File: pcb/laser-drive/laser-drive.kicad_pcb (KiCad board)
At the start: 2 copper layers, 28.6 x 32.4 mm, 28 parts, among them J1 CONN_01X03, P1 LaserOut, Q1 BCP5616Q, Q2 MTM232270, U2 MIC920

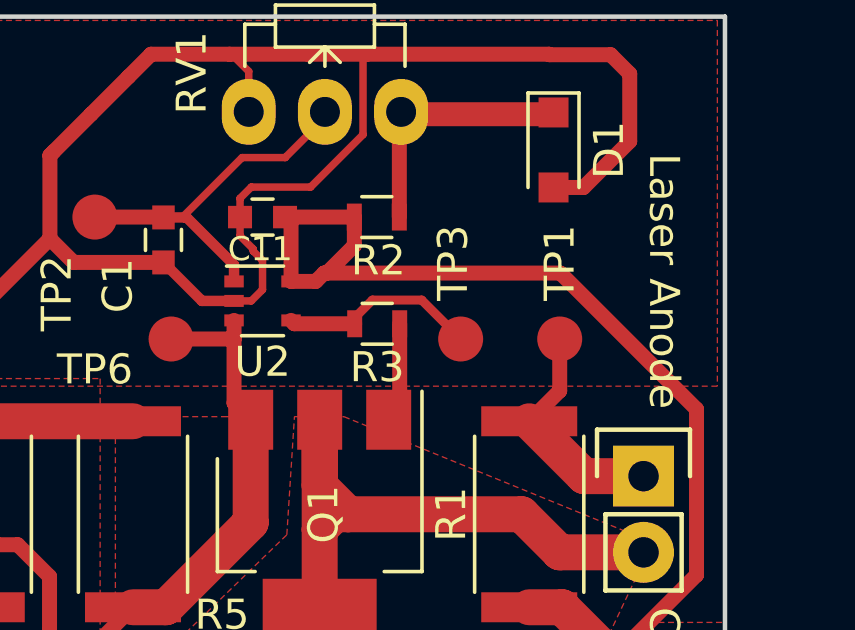
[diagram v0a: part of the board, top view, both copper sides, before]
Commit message: Add oscillation suppresion cap for laser driver.
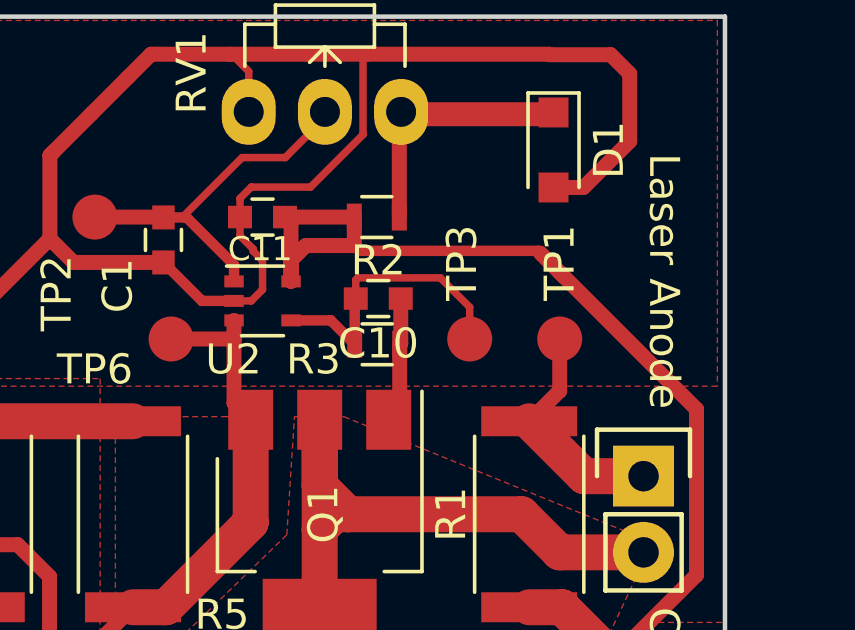
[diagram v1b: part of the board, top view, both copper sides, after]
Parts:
- added C10: 100p, Capacitors_SMD:C_0603, F.Cu at (100.2, 54.5)
- moved R3 0.68 mm to (100.2, 56.0)
- moved TP3 0.30 mm to (103.3, 55.8)
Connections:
- net /ControlOut renamed Net-(C10-Pad2)
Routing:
- net Net-(C10-Pad2): track 6.84 -> 9.93 mm
- net Net-(C10-Pad1): track 3.35 -> 4.21 mm

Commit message: o work in progress.
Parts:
- removed the C5 at (98.1, 75.0)
- removed the C6 at (93.7, 69.9)
- removed the C7 at (98.1, 69.9)
- removed C8: 10u, Capacitors_SMD:C_1210
- removed C9: 100n, Capacitors_SMD:C_0805
- added C2: 100n, Capacitors_SMD:C_0603, F.Cu at (106.2, 73.2)
- added REF**: MountingHole_3.2mm_M3, Mounting_Holes:MountingHole_3.2mm_M3, F.Cu at (94.0, 73.7)
- added REF**: MountingHole_3.2mm_M3, Mounting_Holes:MountingHole_3.2mm_M3, F.Cu at (108.0, 53.3)
- J1: footprint Pin_Headers:Pin_Header_Straight_1x03_Pitch2.54mm -> Pin_Headers:Pin_Header_Straight_1x03_Pitch2.00mm
- P1: footprint Pin_Headers:Pin_Header_Straight_1x02 -> Connectors_JST:JST_XH_B02B-XH-A_02x2.50mm_Straight
- TP1: value Current -> Curr
- TP3: value Control-Out -> Ctrl
- moved TP3 21.8 mm to (124.1, 62.1)
- moved R8 17.1 mm to (106.2, 75.9), turned to 0 degrees
- moved TP6 17.0 mm to (76.3, 57.0)
- moved J1 14.2 mm to (99.1, 75.9), turned to 90 degrees
- moved R3 11.5 mm to (91.2, 63.2), turned to 270 degrees
- moved TP2 10.8 mm to (80.5, 48.3)
- moved C6 10.3 mm to (91.2, 59.4), turned to 270 degrees
- moved Q2 10.1 mm to (99.1, 72.1), turned to 270 degrees
- moved R7 9.79 mm to (94.2, 68.1), turned to 0 degrees
- moved R6 9.61 mm to (99.3, 68.8), turned to 270 degrees
- moved R1 9.39 mm to (102.4, 70.6)
- moved D1 6.77 mm to (102.6, 55.4), turned to 90 degrees
- moved R2 5.69 mm to (95.8, 55.4)
- moved TP1 4.52 mm to (110.5, 57.4)
- moved C7 4.36 mm to (98.8, 55.4)
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- renumbered C2 to C3, C3 to C4, C4 to C5, C10 to C6, C11 to C7
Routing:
- net GND: track 130.9 -> 0.00 mm
- net +12V: track 85.8 -> 0.00 mm, vias 2 -> 0
- net /LaserOut: track 21.4 -> 0.00 mm
- net /VSense: track 17.0 -> 0.00 mm
- net /VRef: track 12.8 -> 0.00 mm
- net Net-(C6-Pad2): track 9.93 -> 0.00 mm
- net Net-(D1-Pad1): track 9.19 -> 0.00 mm
- net /CurrentTP: track 7.73 -> 0.00 mm
- net Net-(Q2-Pad3): track 6.55 -> 0.00 mm
- net Net-(R5-Pad2): track 5.21 -> 0.00 mm
- net Net-(J1-Pad2): track 4.56 -> 0.00 mm
- net Net-(C6-Pad1): track 4.21 -> 0.00 mm
- removed copper zone on F.Cu, net +12V
- removed copper zone on F.Cu, net /LaserOut
- removed copper zone on F.Cu, net /VSense
- removed copper zone on F.Cu, net GND
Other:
- board size 28.6 x 32.4 mm -> 21.6 x 27.9 mm

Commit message: playing with placement.
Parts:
- moved TP1 11.4 mm to (121.9, 57.7)
- moved R8 8.88 mm to (101.7, 68.3), turned to 90 degrees
- moved C3 7.94 mm to (104.9, 68.3), turned to 180 degrees
- moved R1 7.28 mm to (109.6, 69.6)
- moved C5 7.01 mm to (108.9, 75.5), turned to 180 degrees
- moved C4 5.53 mm to (104.9, 71.8), turned to 180 degrees
- moved C2 2.44 mm to (105.7, 75.5), turned to 270 degrees
- moved P1 0.97 mm to (107.6, 62.5)
- moved J1 0.50 mm to (98.6, 75.7)
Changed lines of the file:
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@@
 )
 (setup
-  (last_trace_width 0.3)
+  (last_trace_width 0.25)
   (user_trace_width 0.25)
   (user_trace_width 0.3)
@@
 )
   (module Capacitors_SMD:C_0603 (layer F.Cu)
-    (at 106.172 73.152)
+    (at 105.664 75.5396 270)
     (descr "Capacitor SMD 0603, reflow soldering, AVX (see smccp.pdf)")
     (tags "capacitor 0603")
     (attr smd)
-    (fp_text reference C2 (at 0 -1.5) (layer F.SilkS)
-      (effects (font (size 1 1) (thickness 0.15)))
-    )
-    (fp_text value 100n (at 0 1.5) (layer F.Fab)
+    (fp_text reference C2 (at 0 -1.5 270) (layer F.SilkS)
+      (effects (font (size 1 1) (thickness 0.15)))
+    )
+    (fp_text value 100n (at 0 1.5 270) (layer F.Fab)
       (effects (font (size 1 1) (thickness 0.15)))
     )
@@
     (fp_line (start 0.8 0.4) (end -0.8 0.4) (layer F.Fab) (width 0.1))
     (fp_line (start -0.8 0.4) (end -0.8 -0.4) (layer F.Fab) (width 0.1))
-    (fp_text user %R (at 0 0) (layer F.Fab)
+    (fp_text user %R (at 0 0 270) (layer F.Fab)
       (effects (font (size 0.3 0.3) (thickness 0.075)))
     )
-    (pad 2 smd rect (at 0.75 0) (size 0.8 0.75) (layers F.Cu F.Paste F.Mask)
-      (net 1 GND))
-    (pad 1 smd rect (at -0.75 0) (size 0.8 0.75) (layers F.Cu F.Paste F.Mask)
+    (pad 2 smd rect (at 0.75 0 270) (size 0.8 0.75) (layers F.Cu F.Paste F.Mask)
+      (net 1 GND))
+    (pad 1 smd rect (at -0.75 0 270) (size 0.8 0.75) (layers F.Cu F.Paste F.Mask)
       (net 2 +12V))
     (model Capacitors_SMD.3dshapes/C_0603.wrl
@@
   )
   (module Pin_Headers:Pin_Header_Straight_1x03_Pitch2.00mm (layer F.Cu)
-    (at 99.06 75.946 90)
+    (at 98.6028 75.7428 90)
     (descr "Through hole straight pin header, 1x03, 2.00mm pitch, single row")
     (tags "Through hole pin header THT 1x03 2.00mm single row")
@@
   )
   (module Connectors_JST:JST_XH_B02B-XH-A_02x2.50mm_Straight (layer F.Cu)
-    (at 107.569 63.5 90)
+    (at 107.5944 62.5348 90)
     (descr "JST XH series connector, B02B-XH-A, top entry type, through hole")
     (tags "connector jst xh tht top vertical 2.50mm")
@@
   )
   (module Capacitors_SMD:C_1210 (layer F.Cu)
-    (at 109.728 69.088 90)
+    (at 104.902 71.7804 180)
     (descr "Capacitor SMD 1210, reflow soldering, AVX (see smccp.pdf)")
     (tags "capacitor 1210")
     (attr smd)
-    (fp_text reference C4 (at 0 -2.25 90) (layer F.SilkS)
-      (effects (font (size 1 1) (thickness 0.15)))
-    )
-    (fp_text value 10u (at 0 2.5 90) (layer F.Fab)
+    (fp_text reference C4 (at 0 -2.25 180) (layer F.SilkS)
+      (effects (font (size 1 1) (thickness 0.15)))
+    )
+    (fp_text value 10u (at 0 2.5 180) (layer F.Fab)
       (effects (font (size 1 1) (thickness 0.15)))
     )
@@
     (fp_line (start 1.6 1.25) (end -1.6 1.25) (layer F.Fab) (width 0.1))
     (fp_line (start -1.6 1.25) (end -1.6 -1.25) (layer F.Fab) (width 0.1))
-    (fp_text user %R (at 0 -2.25 90) (layer F.Fab)
-      (effects (font (size 1 1) (thickness 0.15)))
-    )
-    (pad 2 smd rect (at 1.5 0 90) (size 1 2.5) (layers F.Cu F.Paste F.Mask)
-      (net 1 GND))
-    (pad 1 smd rect (at -1.5 0 90) (size 1 2.5) (layers F.Cu F.Paste F.Mask)
+    (fp_text user %R (at 0 -2.25 180) (layer F.Fab)
+      (effects (font (size 1 1) (thickness 0.15)))
+    )
+    (pad 2 smd rect (at 1.5 0 180) (size 1 2.5) (layers F.Cu F.Paste F.Mask)
+      (net 1 GND))
+    (pad 1 smd rect (at -1.5 0 180) (size 1 2.5) (layers F.Cu F.Paste F.Mask)
       (net 2 +12V))
     (model Capacitors_SMD.3dshapes/C_1210.wrl
@@
   )
   (module Capacitors_SMD:C_1210 (layer F.Cu)
-    (at 106.172 69.088 90)
+    (at 108.9152 75.5396 180)
     (descr "Capacitor SMD 1210, reflow soldering, AVX (see smccp.pdf)")
     (tags "capacitor 1210")
     (attr smd)
-    (fp_text reference C5 (at 0 -2.25 90) (layer F.SilkS)
-      (effects (font (size 1 1) (thickness 0.15)))
-    )
-    (fp_text value 10u (at 0 2.5 90) (layer F.Fab)
-      (effects (font (size 1 1) (thickness 0.15)))
-    )
-    (fp_text user %R (at 0 -2.25 90) (layer F.Fab)
+    (fp_text reference C5 (at 0 -2.25 180) (layer F.SilkS)
+      (effects (font (size 1 1) (thickness 0.15)))
+    )
+    (fp_text value 10u (at 0 2.5 180) (layer F.Fab)
+      (effects (font (size 1 1) (thickness 0.15)))
+    )
+    (fp_text user %R (at 0 -2.25 180) (layer F.Fab)
       (effects (font (size 1 1) (thickness 0.15)))
     )
@@
     (fp_line (start 2.25 1.5) (end 2.25 -1.5) (layer F.CrtYd) (width 0.05))
     (fp_line (start 2.25 1.5) (end -2.25 1.5) (layer F.CrtYd) (width 0.05))
-    (pad 1 smd rect (at -1.5 0 90) (size 1 2.5) (layers F.Cu F.Paste F.Mask)
+    (pad 1 smd rect (at -1.5 0 180) (size 1 2.5) (layers F.Cu F.Paste F.Mask)
       (net 2 +12V))
-    (pad 2 smd rect (at 1.5 0 90) (size 1 2.5) (layers F.Cu F.Paste F.Mask)
+    (pad 2 smd rect (at 1.5 0 180) (size 1 2.5) (layers F.Cu F.Paste F.Mask)
       (net 1 GND))
     (model Capacitors_SMD.3dshapes/C_1210.wrl
@@
   )
   (module Capacitors_SMD:C_1210 (layer F.Cu)
-    (at 109.601 74.676 270)
+    (at 104.902 68.2752 180)
     (descr "Capacitor SMD 1210, reflow soldering, AVX (see smccp.pdf)")
     (tags "capacitor 1210")
     (attr smd)
-    (fp_text reference C3 (at 0 -2.25 270) (layer F.SilkS)
-      (effects (font (size 1 1) (thickness 0.15)))
-    )
-    (fp_text value 10u (at 0 2.5 270) (layer F.Fab)
-      (effects (font (size 1 1) (thickness 0.15)))
-    )
-    (fp_text user %R (at 0 -2.25 270) (layer F.Fab)
+    (fp_text reference C3 (at 0 -2.25 180) (layer F.SilkS)
+      (effects (font (size 1 1) (thickness 0.15)))
+    )
+    (fp_text value 10u (at 0 2.5 180) (layer F.Fab)
+      (effects (font (size 1 1) (thickness 0.15)))
+    )
+    (fp_text user %R (at 0 -2.25 180) (layer F.Fab)
       (effects (font (size 1 1) (thickness 0.15)))
     )
@@
     (fp_line (start 2.25 1.5) (end 2.25 -1.5) (layer F.CrtYd) (width 0.05))
     (fp_line (start 2.25 1.5) (end -2.25 1.5) (layer F.CrtYd) (width 0.05))
-    (pad 1 smd rect (at -1.5 0 270) (size 1 2.5) (layers F.Cu F.Paste F.Mask)
+    (pad 1 smd rect (at -1.5 0 180) (size 1 2.5) (layers F.Cu F.Paste F.Mask)
       (net 2 +12V))
-    (pad 2 smd rect (at 1.5 0 270) (size 1 2.5) (layers F.Cu F.Paste F.Mask)
+    (pad 2 smd rect (at 1.5 0 180) (size 1 2.5) (layers F.Cu F.Paste F.Mask)
       (net 1 GND))
     (model Capacitors_SMD.3dshapes/C_1210.wrl
@@
   )
   (module Measurement_Points:Measurement_Point_Round-SMD-Pad_Small (layer F.Cu)
-    (at 110.49 57.404 270)
+    (at 121.8692 57.658 270)
     (descr "Mesurement Point, Round, SMD Pad, DM 1.5mm,")
     (tags "Mesurement Point Round SMD Pad 1.5mm")
@@
   )
   (module Resistors_SMD:R_0603 (layer F.Cu)
-    (at 106.172 75.946)
+    (at 101.7016 68.2752 90)
     (descr "Resistor SMD 0603, reflow soldering, Vishay (see dcrcw.pdf)")
     (tags "resistor 0603")
     (attr smd)
-    (fp_text reference R8 (at -2.413 -0.889) (layer F.SilkS)
-      (effects (font (size 1 1) (thickness 0.15)))
-    )
-    (fp_text value 1k (at 0 1.5) (layer F.Fab)
-      (effects (font (size 1 1) (thickness 0.15)))
-    )
-    (fp_text user %R (at 0 -1.45) (layer F.Fab)
+    (fp_text reference R8 (at -2.413 -0.889 90) (layer F.SilkS)
+      (effects (font (size 1 1) (thickness 0.15)))
+    )
+    (fp_text value 1k (at 0 1.5 90) (layer F.Fab)
+      (effects (font (size 1 1) (thickness 0.15)))
+    )
+    (fp_text user %R (at 0 -1.45 90) (layer F.Fab)
       (effects (font (size 1 1) (thickness 0.15)))
     )
@@
     (fp_line (start 1.25 0.7) (end 1.25 -0.7) (layer F.CrtYd) (width 0.05))
     (fp_line (start 1.25 0.7) (end -1.25 0.7) (layer F.CrtYd) (width 0.05))
-    (pad 1 smd rect (at -0.75 0) (size 0.5 0.9) (layers F.Cu F.Paste F.Mask)
-      (net 1 GND))
-    (pad 2 smd rect (at 0.75 0) (size 0.5 0.9) (layers F.Cu F.Paste F.Mask)
+    (pad 1 smd rect (at -0.75 0 90) (size 0.5 0.9) (layers F.Cu F.Paste F.Mask)
+      (net 1 GND))
+    (pad 2 smd rect (at 0.75 0 90) (size 0.5 0.9) (layers F.Cu F.Paste F.Mask)
       (net 10 "Net-(J1-Pad2)"))
     (model Resistors_SMD.3dshapes/R_0603.wrl
@@
   )
   (module Resistors_SMD:R_2512 (layer F.Cu)
-    (at 102.362 70.612 90)
+    (at 109.5756 69.596 90)
     (descr "Resistor SMD 2512, reflow soldering, Vishay (see dcrcw.pdf)")
     (tags "resistor 2512")
